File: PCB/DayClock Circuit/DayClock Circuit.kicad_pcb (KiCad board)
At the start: 2 copper layers, 28 parts, among them J10 Conn_02x08_Odd_Even, J11 Conn_01x02, J3 molex 15-24-4441, J5 4002 LCD Screen, J6 Encoder, J7 RGB_LED_Strip_Connector, J8 RGB_LED_Strip_Connector, J9 RGB_LED_Strip_Connector, Q1 N-MOSFET, Q2 N-MOSFET, Q3 N-MOSFET, Q4 N-MOSFET, Q5 N-MOSFET, Q6 N-MOSFET, Q7 N-MOSFET, Q8 N-MOSFET, Q9 N-MOSFET, U1 Tiny_RTC_DS1307

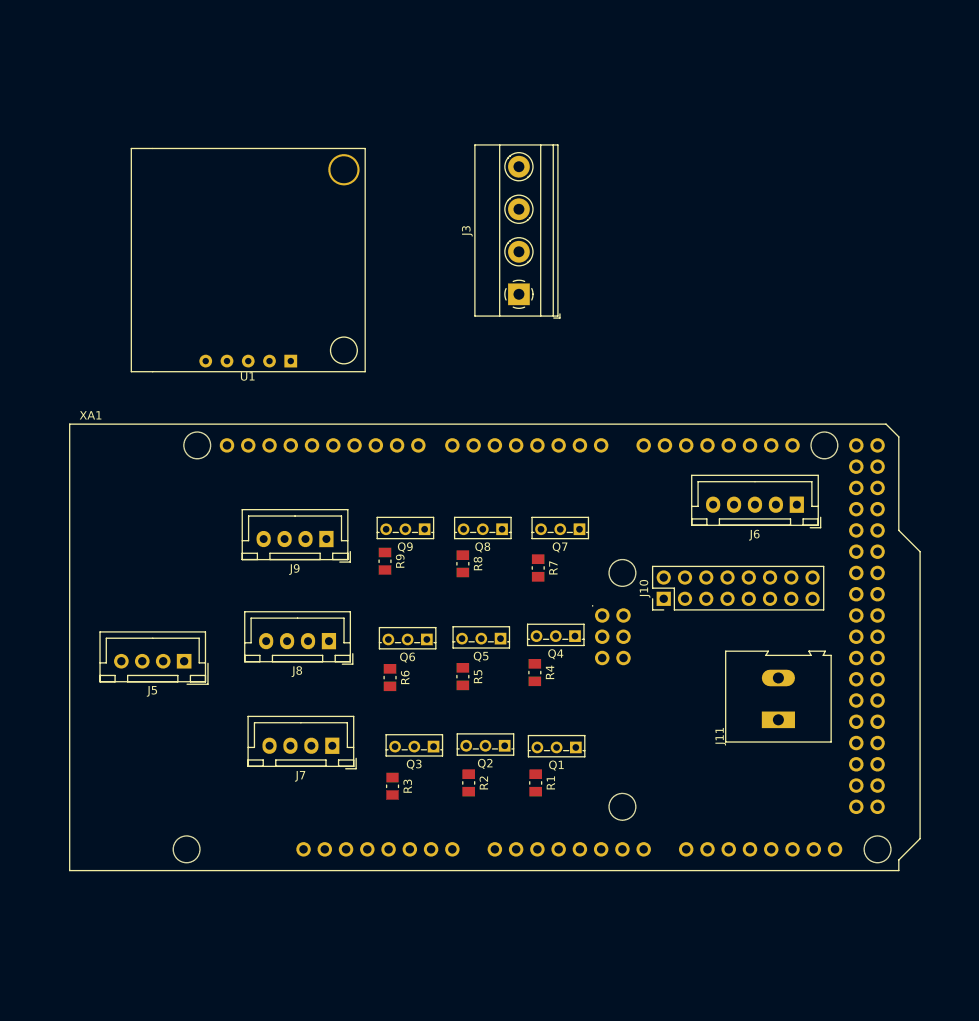
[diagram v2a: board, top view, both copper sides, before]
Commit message: Added thick power traces and design rules.
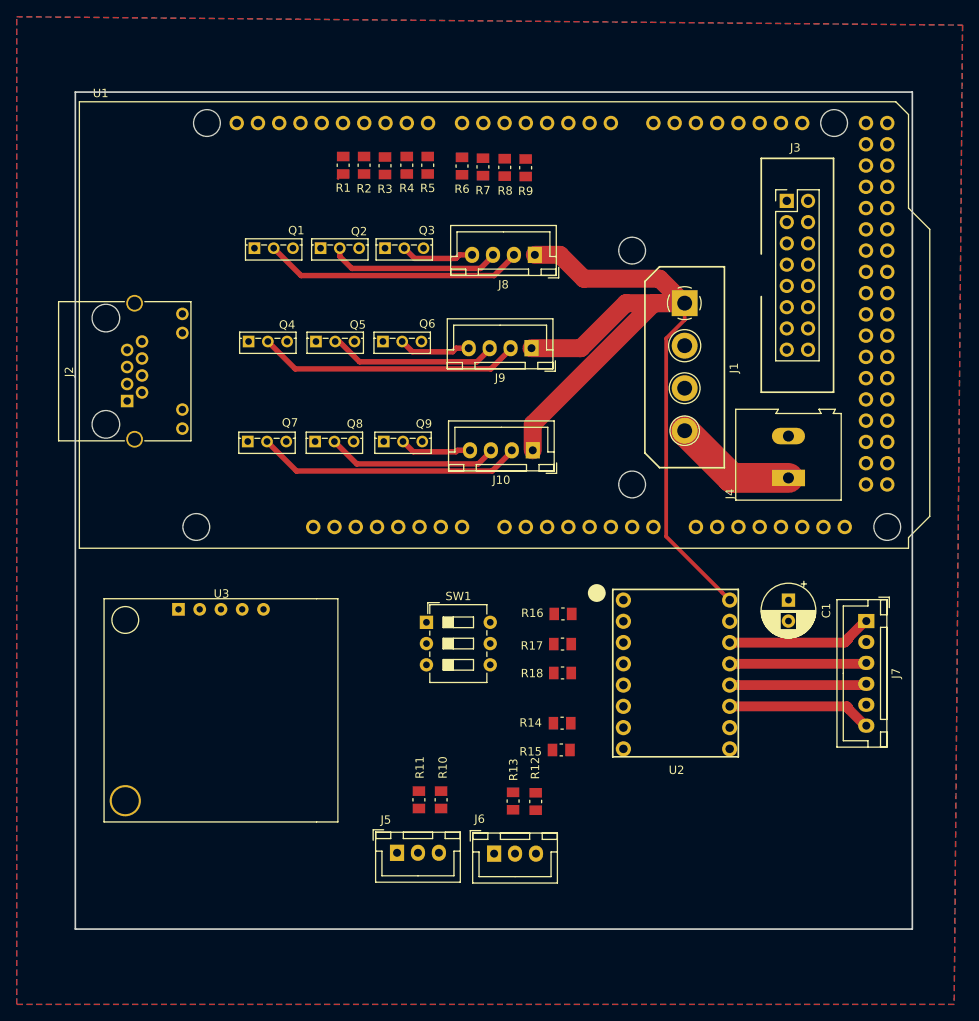
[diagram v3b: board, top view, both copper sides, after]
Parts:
- removed J11: Conn_01x02, TerminalBlock:TerminalBlock_Altech_AK300-2_P5.00mm
- removed XA1: Arduino_Mega2560_Shield, Arduino:Arduino_Mega2560_Shield
- added C1: 100uF, Capacitor_THT:CP_Radial_D6.3mm_P2.50mm, F.Cu at (100.2, 75.7)
- added J1: molex 15-24-4441, rich-footprints:Molex_15-24-4449_ATX_Power_Supply_Connector, F.Cu at (87.8, 47.9)
- added J2: RJ45, Connector_RJ:RJ45_Amphenol_RJHSE538X, F.Cu at (21.2, 51.9)
- added J4: LED Matrix Power, TerminalBlock:TerminalBlock_Altech_AK300-2_P5.00mm, F.Cu at (100.2, 61.1)
- added R10: 10k, Resistor_SMD:R_0805_2012Metric_Pad1.15x1.50mm_HandSolder, F.Cu at (58.7, 99.6)
- added R11: 6.8k, Resistor_SMD:R_0805_2012Metric_Pad1.15x1.50mm_HandSolder, F.Cu at (56.0, 99.6)
- added R12: 10k, Resistor_SMD:R_0805_2012Metric_Pad1.15x1.50mm_HandSolder, F.Cu at (70.0, 99.8)
- added R13: 6.8k, Resistor_SMD:R_0805_2012Metric_Pad1.15x1.50mm_HandSolder, F.Cu at (67.3, 99.7)
- added R14: 10k, Resistor_SMD:R_0805_2012Metric_Pad1.15x1.50mm_HandSolder, F.Cu at (73.2, 90.4)
- added R15: 10k, Resistor_SMD:R_0805_2012Metric_Pad1.15x1.50mm_HandSolder, F.Cu at (73.1, 93.6)
- added R16: 10k, Resistor_SMD:R_0805_2012Metric_Pad1.15x1.50mm_HandSolder, F.Cu at (73.3, 77.3)
- added R17: 10k, Resistor_SMD:R_0805_2012Metric_Pad1.15x1.50mm_HandSolder, F.Cu at (73.2, 81.0)
- added R18: 10k, Resistor_SMD:R_0805_2012Metric_Pad1.15x1.50mm_HandSolder, F.Cu at (73.2, 84.4)
- added SW1: SW_DIP_x03, Button_Switch_THT:SW_DIP_SPSTx03_Slide_6.7x9.18mm_W7.62mm_P2.54mm_LowProfile, F.Cu at (57.0, 78.3)
- added U2: DRV8825_module, rich-footprints:DRV8825_board, F.Cu at (88.1, 85.8)
- added U3: Tiny_RTC_DS1307, rich-footprints:TinyRTC-one-mounting-hole, F.Cu at (17.2, 79.3)
- J10: value Conn_02x08_Odd_Even -> RGB_LED_Strip_Connector; footprint Connector_PinHeader_2.54mm:PinHeader_2x08_P2.54mm_Vertical -> Connector_JST:JST_XH_B04B-XH-A_1x04_P2.50mm_Vertical
- J3: value molex 15-24-4441 -> Conn_02x08_Odd_Even; footprint TerminalBlock_Phoenix:TerminalBlock_Phoenix_MKDS-1,5-4-5.08_1x04_P5.08mm_Horizontal -> rich-footprints:3M_Header_2x8_Keyed
- J5: value 4002 LCD Screen -> Lower Limit Switch; footprint Connectors_JST:JST_XH_B04B-XH-A_04x2.50mm_Straight -> Connector_JST:JST_XH_B03B-XH-A_1x03_P2.50mm_Vertical
- J6: value Encoder -> Upper Limit Switch; footprint Connector_JST:JST_XH_B05B-XH-A_1x05_P2.50mm_Vertical -> Connector_JST:JST_XH_B03B-XH-A_1x03_P2.50mm_Vertical
- J7: value RGB_LED_Strip_Connector -> Stepper Motor; footprint Connector_JST:JST_XH_B04B-XH-A_1x04_P2.50mm_Vertical -> Connector_JST:JST_XH_B06B-XH-A_1x06_P2.50mm_Vertical
- U1: value Tiny_RTC_DS1307 -> Arduino_Mega2560_Shield; footprint rich-footprints:TinyRTC-one-mounting-hole -> rich-footprints:Arduino_Mega2560_Shield_No_Serial_Header
- moved R1 77.3 mm to (47.0, 23.7), turned to 90 degrees
- moved R2 74.9 mm to (49.5, 23.7), turned to 90 degrees
- moved R3 74.1 mm to (52.0, 23.8), turned to 90 degrees
- moved Q1 70.9 mm to (36.4, 33.6), turned to 0 degrees
- moved J7 65.5 mm to (109.5, 78.2), turned to 270 degrees
- moved Q2 63.4 mm to (44.3, 33.6), turned to 0 degrees
- moved R4 62.5 mm to (54.6, 23.7), turned to 90 degrees
- moved R6 61.7 mm to (61.2, 23.8), turned to 90 degrees
- moved R5 61.2 mm to (57.1, 23.7), turned to 90 degrees
- moved Q3 59.8 mm to (52.0, 33.6), turned to 0 degrees
- moved J6 55.2 mm to (65.0, 106.0), turned to 0 degrees
- moved Q4 52.5 mm to (35.7, 44.8), turned to 0 degrees
- moved J8 52.3 mm to (69.9, 34.5)
- moved R9 49.9 mm to (68.8, 24.0), turned to 90 degrees
- moved R7 48.4 mm to (63.7, 23.9), turned to 90 degrees
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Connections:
- J10 pad 1: /D24 -> +12V
- J10 pad 2: /D25 -> Net-(J10-Pad2)
- J10 pad 3: /D26 -> Net-(J10-Pad3)
- J10 pad 4: GND -> Net-(J10-Pad4)
- J3 pad 1: +12V -> /D24
- J3 pad 2: GND -> /D25
- J3 pad 3: GND -> /D26
- J3 pad 4: +5V -> GND
- J5 pad 1: GND -> +12V
- J5 pad 2: +5V -> GND
- J5 pad 3: /SDA -> Net-(J5-Pad3)
- J6 pad 1: GND -> +12V
- J6 pad 2: +5V -> GND
- J6 pad 3: /D19 -> Net-(J6-Pad3)
- J7 pad 1: +12V -> Net-(J7-Pad1)
- J7 pad 2: Net-(J7-Pad2) -> (no net)
- Q1 pad 1: /D2 -> /D12
- Q1 pad 2: Net-(J7-Pad2) -> Net-(J8-Pad2)
- Q2 pad 1: /D3 -> /D11
- Q2 pad 2: Net-(J7-Pad3) -> Net-(J8-Pad3)
- Q3 pad 1: /D4 -> /D10
- Q3 pad 2: Net-(J7-Pad4) -> Net-(J8-Pad4)
- Q4 pad 1: /D5 -> /D9
- Q4 pad 2: Net-(J8-Pad2) -> Net-(J9-Pad2)
- Q5 pad 1: /D6 -> /D8
- Q5 pad 2: Net-(J8-Pad3) -> Net-(J9-Pad3)
- Q6 pad 2: Net-(J8-Pad4) -> Net-(J9-Pad4)
- Q7 pad 1: /D8 -> /D6
- Q7 pad 2: Net-(J9-Pad2) -> Net-(J10-Pad2)
- Q8 pad 1: /D9 -> /D5
- Q8 pad 2: Net-(J9-Pad3) -> Net-(J10-Pad3)
- Q9 pad 1: /D10 -> /D4
- Q9 pad 2: Net-(J9-Pad4) -> Net-(J10-Pad4)
- R1 pad 2: /D2 -> /D12
- R2 pad 2: /D3 -> /D11
- R3 pad 2: /D4 -> /D10
- R4 pad 2: /D5 -> /D9
- R5 pad 2: /D6 -> /D8
- R7 pad 2: /D8 -> /D6
- R8 pad 2: /D9 -> /D5
- R9 pad 2: /D10 -> /D4
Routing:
- net +12V: track 0.00 -> 107.6 mm
- net Net-(J10-Pad2): track 0.00 -> 31.8 mm
- net Net-(J9-Pad2): track 0.00 -> 31.5 mm
- net Net-(J8-Pad2): track 0.00 -> 31.2 mm
- net Net-(J8-Pad3): track 0.00 -> 20.6 mm
- net Net-(J10-Pad3): track 0.00 -> 20.6 mm
- net Net-(J9-Pad3): track 0.00 -> 20.2 mm
- net Net-(J7-Pad1): track 0.00 -> 17.5 mm
- net Net-(J7-Pad6): track 0.00 -> 17.4 mm
- net Net-(J7-Pad4): track 0.00 -> 16.4 mm
- net Net-(J7-Pad3): track 0.00 -> 16.4 mm
- net +5V: track 0.00 -> 14.7 mm
- net Net-(J8-Pad4): track 0.00 -> 8.78 mm
- net Net-(J9-Pad4): track 0.00 -> 8.63 mm
- net Net-(J10-Pad4): track 0.00 -> 8.58 mm
- added copper zone on B.Cu, net GND
- added copper zone on F.Cu, net GND
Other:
- board outline added: 100 x 100 mm
- net class 12v added: clearance 0.2, trace_width 1.1, via_dia 0.8, via_drill 0.4
- net class 5v added: clearance 0.2, trace_width 3.57, via_dia 0.8, via_drill 0.4
- net class Default: trace_width 0.25 -> 0.2
- net class RGB pins added: clearance 0.2, trace_width 0.65, via_dia 0.8, via_drill 0.4
- net class Stepper J7 added: clearance 0.2, trace_width 1.17, via_dia 0.8, via_drill 0.4

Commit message: Started on signal wires
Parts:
- moved R7 17.7 mm to (46.0, 23.0)
- moved R3 17.6 mm to (69.6, 23.4)
- moved R8 17.3 mm to (49.0, 23.1)
- moved R2 17.2 mm to (66.7, 23.3)
- moved R9 16.8 mm to (52.0, 23.1)
- moved R1 16.7 mm to (63.7, 23.3)
- moved J2 2.41 mm to (23.6, 52.0)
- moved R5 0.86 mm to (57.8, 23.2)
- moved R6 0.64 mm to (60.8, 23.3)
- moved R4 0.54 mm to (54.8, 23.2)
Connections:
- Q1 pad 1: /D12 -> /D6
- Q2 pad 1: /D11 -> /D5
- Q3 pad 1: /D10 -> /D4
- Q7 pad 1: /D6 -> /D12
- Q8 pad 1: /D5 -> /D11
- Q9 pad 1: /D4 -> /D10
- R1 pad 2: /D12 -> /D6
- R2 pad 2: /D11 -> /D5
- R3 pad 2: /D10 -> /D4
- R7 pad 2: /D6 -> /D12
- R8 pad 2: /D5 -> /D11
- R9 pad 2: /D4 -> /D10
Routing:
- net /D10: track 0.00 -> 62.1 mm
- net /D7: track 0.00 -> 57.6 mm
- net /D11: track 0.00 -> 53.4 mm
- net /D8: track 0.00 -> 48.6 mm
- net /D12: track 0.00 -> 46.4 mm
- net /D9: track 0.00 -> 42.2 mm
- net /D6: track 0.00 -> 38.7 mm
- net /D5: track 0.00 -> 33.7 mm
- net /D4: track 0.00 -> 31.3 mm
- net /D31: track 0.00 -> 21.5 mm
- net /D29: track 0.00 -> 14.8 mm
- net /D27: track 0.00 -> 14.8 mm
- net /D30: track 0.00 -> 14.7 mm
- net /D24: track 0.00 -> 11.8 mm
- net /D26: track 0.00 -> 11.2 mm
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
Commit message: Giant Day Cycle Clock Rev 1A sent to fab and components ordered
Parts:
- added J11: Breakout Pins, Connector_PinHeader_2.54mm:PinHeader_1x10_P2.54mm_Vertical, F.Cu at (105.9, 17.1)
- added REF**: MountingHole_3.2mm_M3, MountingHole:MountingHole_3.2mm_M3, F.Cu at (20.0, 95.0)
- added REF**: MountingHole_3.2mm_M3, MountingHole:MountingHole_3.2mm_M3, F.Cu at (99.0, 96.0)
- U3: footprint rich-footprints:TinyRTC-one-mounting-hole -> rich-footprints:TinyRTC-coin-side-up
- moved J5 86.0 mm to (92.2, 29.1), turned to 180 degrees
- moved J6 78.6 mm to (81.0, 29.1), turned to 180 degrees
- moved R11 73.7 mm to (94.3, 36.5), turned to 90 degrees
- moved R10 71.1 mm to (91.7, 36.5), turned to 270 degrees
- moved R13 66.6 mm to (88.0, 36.4), turned to 90 degrees
- moved R12 65.2 mm to (85.3, 36.3), turned to 270 degrees
- moved U3 40.2 mm to (55.6, 91.1), turned to 90 degrees
- moved J2 4.75 mm to (19.8, 54.9)
- moved R18 4.65 mm to (73.9, 89.0)
- moved R17 4.31 mm to (73.9, 85.2)
- moved R16 4.12 mm to (74.0, 81.4)
- moved C1 4.03 mm to (98.6, 79.4)
- moved R7 3.88 mm to (45.3, 26.9)
- moved R8 3.85 mm to (48.4, 26.9)
- moved U2 3.83 mm to (87.6, 89.7)
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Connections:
- U1 pad 5V3: (no net) -> /5V3
- U1 pad D0: (no net) -> /D0
- U1 pad D1: (no net) -> /D1
- U1 pad D14: (no net) -> /D14
- U1 pad D15: (no net) -> /D15
- U1 pad D16: (no net) -> /D16
- U1 pad D20: (no net) -> /D20
- U1 pad D21: (no net) -> /D21
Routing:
- net +5V: track 14.7 -> 166.1 mm, vias 0 -> 2
- net /D22: track 0.00 -> 113.7 mm, vias 0 -> 2
- net /D19: track 0.00 -> 105.1 mm
- net /D34: track 0.00 -> 103.0 mm
- net /D18: track 0.00 -> 100.9 mm
- net /D17: track 0.00 -> 100.8 mm
- net /D35: track 0.00 -> 98.4 mm
- net /SDA: track 0.00 -> 94.6 mm, vias 0 -> 4
- net /D36: track 0.00 -> 90.7 mm
- net /SCL: track 0.00 -> 88.5 mm
- net +12V: track 107.6 -> 191.0 mm, vias 0 -> 2
- net /D13: track 0.00 -> 73.3 mm, vias 0 -> 1
- net /A0: track 0.00 -> 48.8 mm
- net /A1: track 0.00 -> 46.8 mm
- net /A3: track 0.00 -> 40.8 mm
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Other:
- board size 100 x 100 mm -> 100 x 85 mm
- net class 12v: trace_width 1.1 -> 0.8
- net class 5v: trace_width 3.57 -> 0.8
- board text added: "0"
- board text added: "1"
- board text added: "12V"
- board text added: "14"
- board text added: "15"
- board text added: "16"
- board text added: "20"
- board text added: "21"
- board text added: "32x64 LED Matrix"
- board text added: "5V"
- board text added: "A1"
- board text added: "A2"
- board text added: "ATX Power Input"
- board text added: "B1"
- board text added: "B2"
- board text added: "Control Box Connector"
- board text added: "DRV8825"
- board text added: "GND"
- board text added: "Giant Day Cycle Clock Rev 1A"
- board text added: "Lower Limit"
- board text added: "M0"
- board text added: "M0 0 1 0 1 0 1"
- board text added: "M1"
- board text added: "M1 0 0 1 1 0 0"
- board text added: "M2"
- board text added: "M2 0 0 0 0 1 1"
- board text added: "Matrix Power"
- board text added: "RGB LED Strip 1"
- board text added: "RGB LED Strip 2"
- board text added: "RGB LED Strip 3"
- board text added: "RTC"
- board text added: "Rich Nelson 06/2018"
- board text added: "Stepper Connector"
- board text added: "Stepper Driver"
- board text added: "Steps Full Half 1/4 1/8 1/16 1/32"
- board text added: "Upper Limit"
